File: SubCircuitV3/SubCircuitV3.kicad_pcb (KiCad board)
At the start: 2 copper layers, 120 x 120.1 mm, 26 parts, among them J1 JTAG, J10 ESC_POWER, J11 ESC_POWER, J12 ESC_POWER, J13 ESC_POWER, J14 FEMALE XT-60, J15 ESC PWM, J16 3S, J2 ESC PWM, J3 ESC PWM, J4 ESC PWM, J5 ESC PWM, J6 ESC PWM, J7 5S, J8 ESC_POWER, J9 ESC_POWER, K1 G5Q-1A

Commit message: Finalized V3 Board
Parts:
- added R3: 1000, Resistor_THT:R_Axial_DIN0207_L6.3mm_D2.5mm_P10.16mm_Horizontal, F.Cu at (107.3, 124.1)
- R1: value 2000 -> 1000
- moved R1 12.5 mm to (111.4, 124.1), turned to -90 degrees
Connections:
- J1 pad 14: Net-(CR1-INPUT) -> Net-(CR1-OUTPUT)
- R1 pad 1: +12V -> Net-(K1-Pad1)
- R1 pad 2: Net-(K1-Pad1) -> +12V
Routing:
- net +12V: track 424.2 -> 435.5 mm
- net Net-(K1-Pad1): track 17.1 -> 22.2 mm
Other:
- board size 120 x 120.1 mm -> 121.4 x 121.2 mm

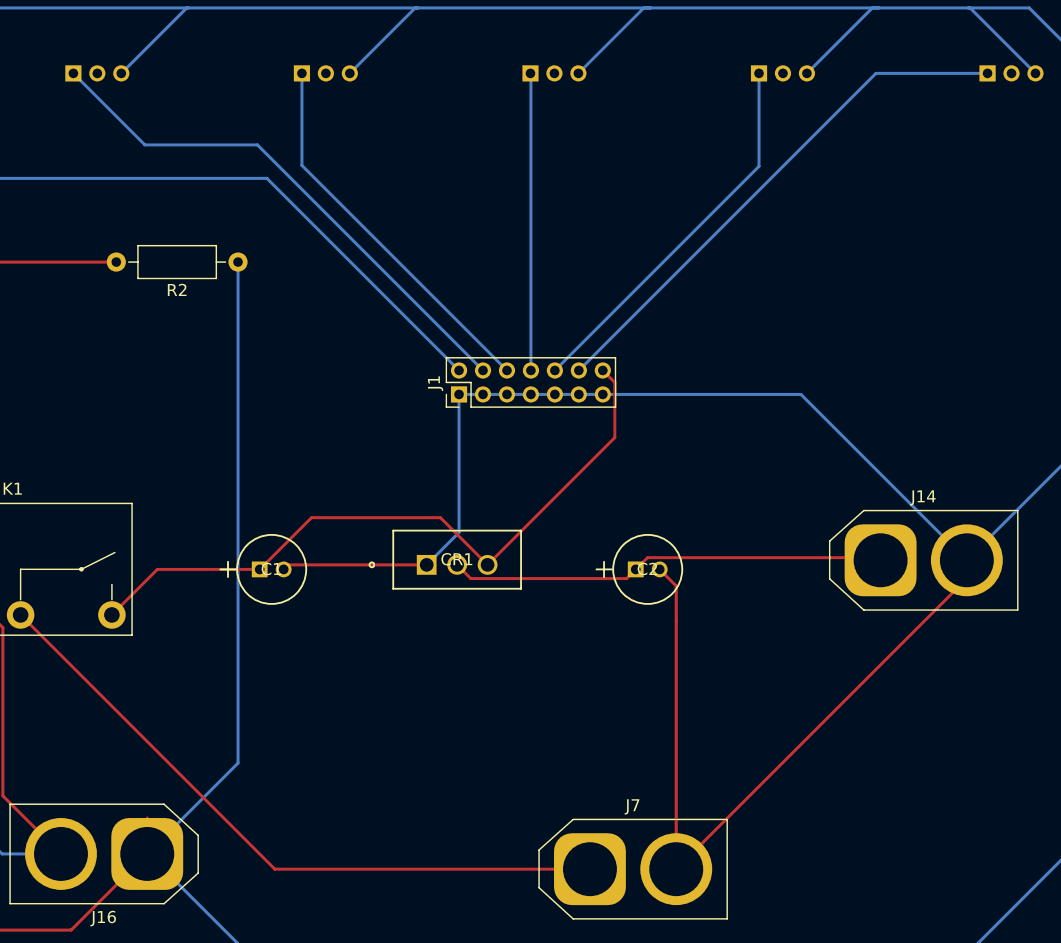
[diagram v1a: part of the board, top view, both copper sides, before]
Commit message: Added water sensors and fixed JTAG-Capacitor connection error
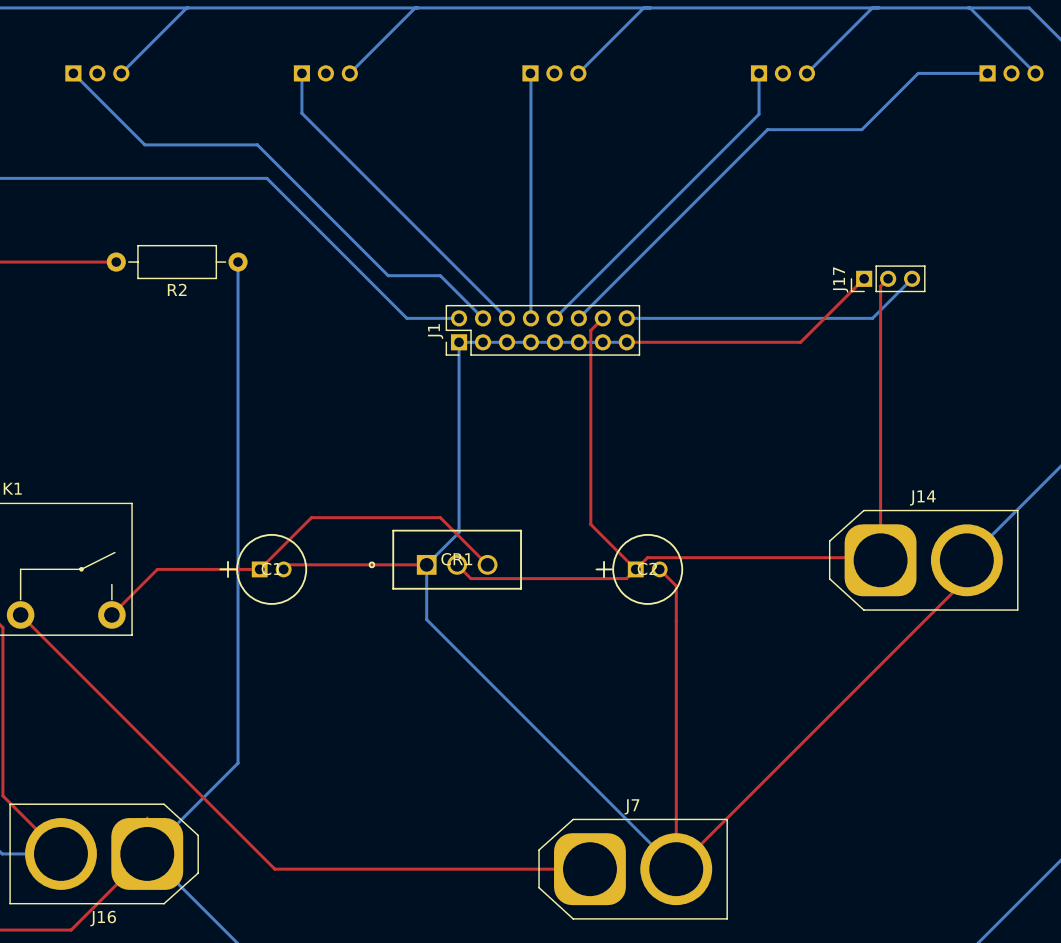
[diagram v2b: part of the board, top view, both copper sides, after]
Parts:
- added J17: Water Sensor Input, Connector_PinHeader_2.00mm:PinHeader_1x03_P2.00mm_Vertical, F.Cu at (196.8, 79.9)
- J1: footprint Connector_PinHeader_2.00mm:PinHeader_2x07_P2.00mm_Vertical -> Connector_PinHeader_2.00mm:PinHeader_2x08_P2.00mm_Vertical
- moved J1 4.35 mm to (163.0, 85.2)
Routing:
- net Net-(CR1-OUTPUT): track 36.6 -> 83.3 mm
- net GND2: track 326.2 -> 352.5 mm
- net Net-(J1-Pin_16): track 0.00 -> 25.2 mm
- net Net-(CR1-INPUT): track 57.4 -> 36.3 mm
- net Net-(J1-Pin_10): track 31.9 -> 27.5 mm
- net Net-(J1-Pin_6): track 31.9 -> 27.7 mm
- net Net-(J1-Pin_8): track 24.9 -> 20.7 mm
- net Net-(J1-Pin_4): track 44.5 -> 42.7 mm
- net Net-(J1-Pin_2): track 61.5 -> 59.7 mm
- net Net-(J1-Pin_12): track 44.4 -> 42.6 mm

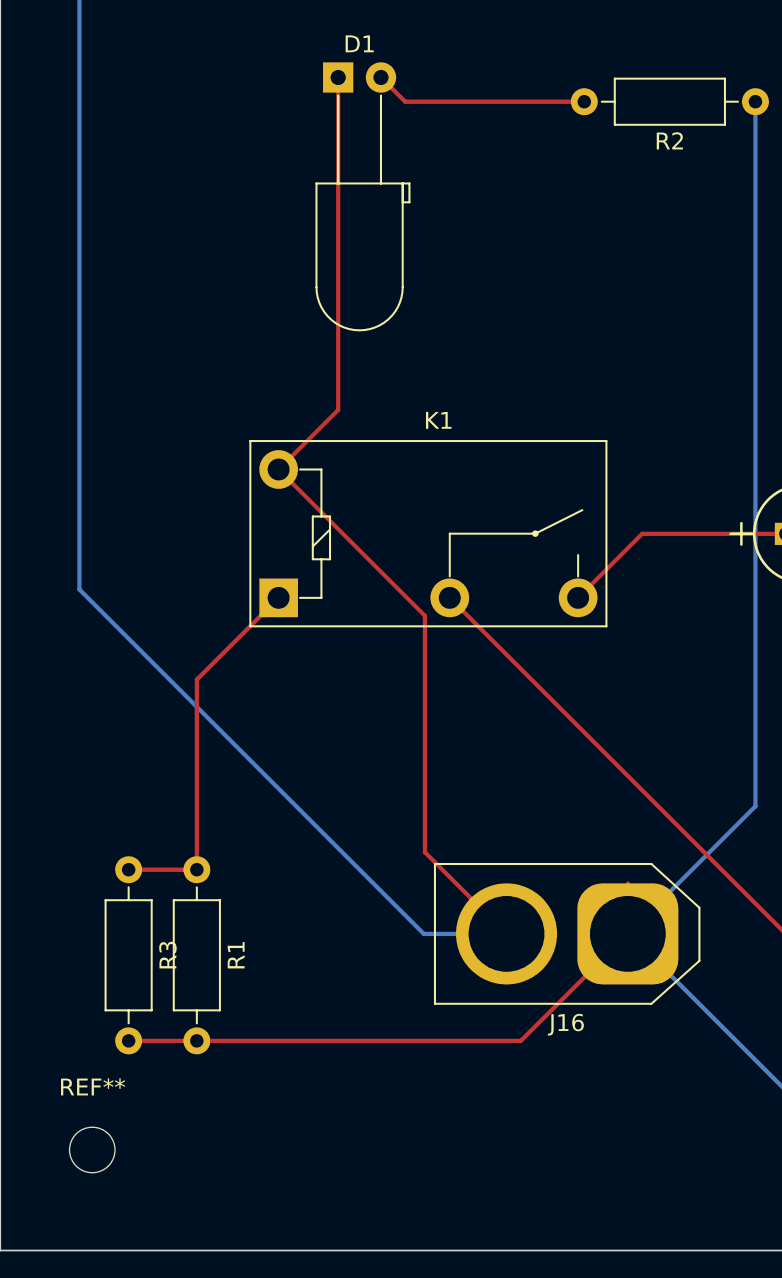
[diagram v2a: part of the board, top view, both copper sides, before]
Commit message: Added mosfet
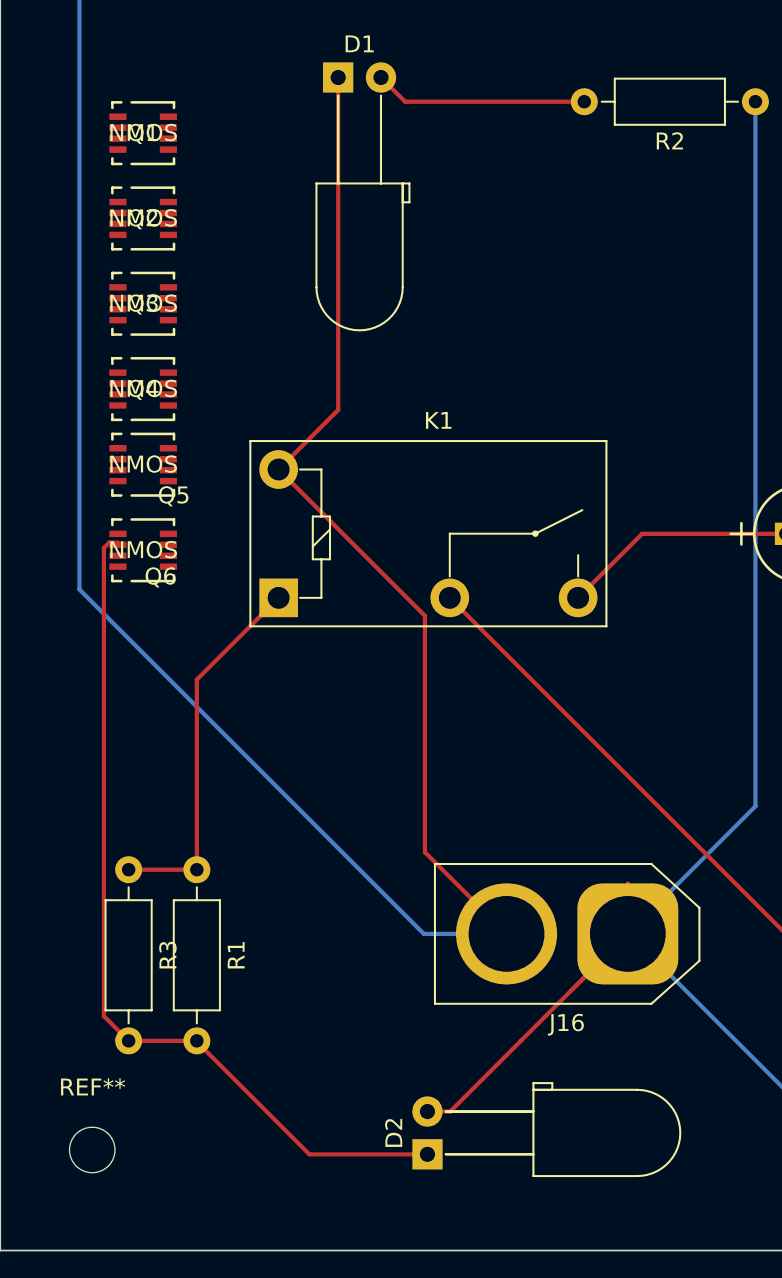
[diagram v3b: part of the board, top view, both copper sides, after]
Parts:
- added D2: switch, LED_THT:LED_D5.0mm_Horizontal_O6.35mm_Z9.0mm, F.Cu at (125.1, 141.0)
- added Q1: NMOS, BSZ065N03LSATMA1-MOSFET:BSZ065N03LSATMA1, F.Cu at (108.2, 80.4)
- added Q2: NMOS, BSZ065N03LSATMA1-MOSFET:BSZ065N03LSATMA1, F.Cu at (108.2, 85.4)
- added Q3: NMOS, BSZ065N03LSATMA1-MOSFET:BSZ065N03LSATMA1, F.Cu at (108.2, 90.5)
- added Q4: NMOS, BSZ065N03LSATMA1-MOSFET:BSZ065N03LSATMA1, F.Cu at (108.2, 95.5)
- added Q5: NMOS, BSZ065N03LSATMA1-MOSFET:BSZ065N03LSATMA1, F.Cu at (108.2, 100.0)
- added Q6: NMOS, BSZ065N03LSATMA1-MOSFET:BSZ065N03LSATMA1, F.Cu at (108.2, 105.1)
- C1, C2: footprint 860010372001:CAP_WCAP-ATG8_5x11_WRE -> Capacitor_WCAP-ATG8_5x11_WRE:CAP_WCAP-ATG8_5x11_WRE
- CR1: footprint LD1085V50_footprints:TO-220_STM -> LD1085V50:TO-220_STM
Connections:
- J10 pad 2: +12V -> Net-(J10-Pin_2)
- J11 pad 2: +12V -> Net-(J11-Pin_2)
- J12 pad 2: +12V -> Net-(J12-Pin_2)
- J13 pad 2: +12V -> Net-(J13-Pin_2)
- J8 pad 2: +12V -> Net-(J8-Pin_2)
- J9 pad 2: +12V -> Net-(J9-Pin_2)
- R1 pad 2: +12V -> /SG
- R3 pad 2: +12V -> /SG
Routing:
- net /SG: track 0.00 -> 50.8 mm
- net +12V: track 435.5 -> 424.2 mm

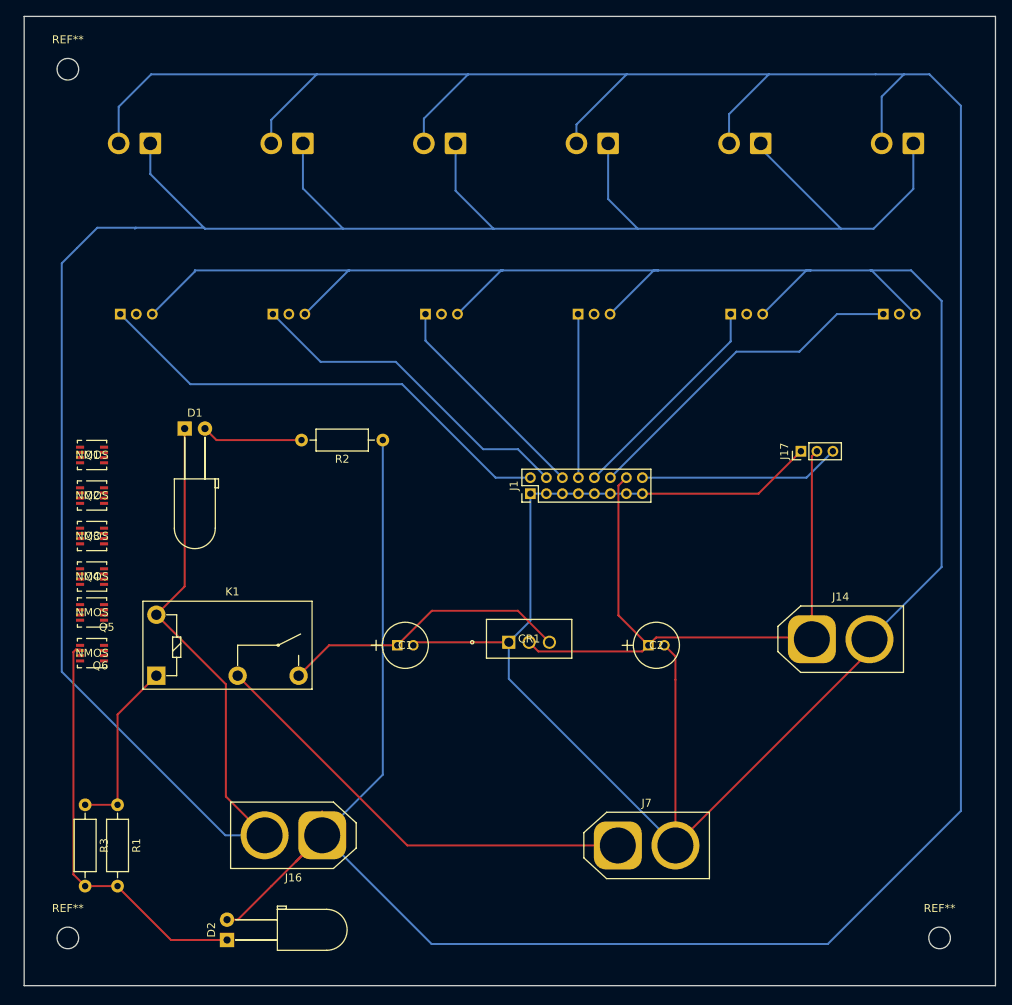
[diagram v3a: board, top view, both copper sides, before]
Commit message: Added fuses, mosfets, and updated power ports
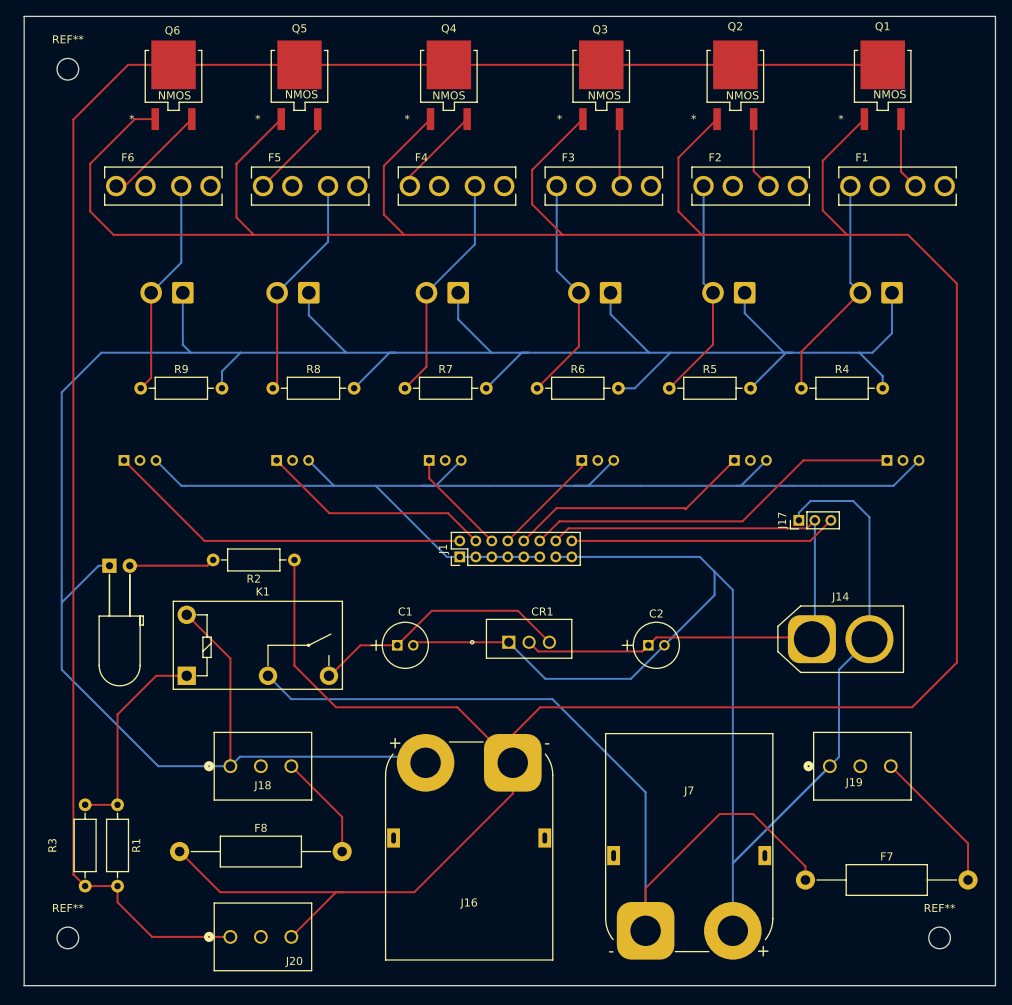
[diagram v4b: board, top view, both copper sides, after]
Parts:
- removed D2: switch, LED_THT:LED_D5.0mm_Horizontal_O6.35mm_Z9.0mm
- added F1: 3544-2, 3544-2:FUSE_3544-2, F.Cu at (208.9, 46.7)
- added F2: 3544-2, 3544-2:FUSE_3544-2, F.Cu at (190.5, 46.7)
- added F3: 3544-2, 3544-2:FUSE_3544-2, F.Cu at (172.2, 46.7)
- added F4: 3544-2, 3544-2:FUSE_3544-2, F.Cu at (153.8, 46.7)
- added F5: 3544-2, 3544-2:FUSE_3544-2, F.Cu at (135.4, 46.7)
- added F6: 3544-2, 3544-2:FUSE_3544-2, F.Cu at (117.1, 46.7)
- added F7: Fuse, Resistor_THT:R_Axial_DIN0411_L9.9mm_D3.6mm_P20.32mm_Horizontal, F.Cu at (197.4, 133.5)
- added F8: Fuse, Resistor_THT:R_Axial_DIN0411_L9.9mm_D3.6mm_P20.32mm_Horizontal, F.Cu at (119.1, 129.9)
- added J18: 3S OUT, 284932-3:CONN3_284392-3_TEC, F.Cu at (125.5, 119.3)
- added J19: 2S OUT, 284932-3:CONN3_284392-3_TEC, F.Cu at (200.4, 119.3)
- added J20: SWITCH, 284932-3:CONN3_284392-3_TEC, F.Cu at (125.5, 140.6)
- added R4: R, Resistor_THT:R_Axial_DIN0207_L6.3mm_D2.5mm_P10.16mm_Horizontal, F.Cu at (196.8, 72.0)
- added R5: R, Resistor_THT:R_Axial_DIN0207_L6.3mm_D2.5mm_P10.16mm_Horizontal, F.Cu at (180.3, 72.0)
- added R6: R, Resistor_THT:R_Axial_DIN0207_L6.3mm_D2.5mm_P10.16mm_Horizontal, F.Cu at (163.8, 72.0)
- added R7: R, Resistor_THT:R_Axial_DIN0207_L6.3mm_D2.5mm_P10.16mm_Horizontal, F.Cu at (147.3, 72.0)
- added R8: R, Resistor_THT:R_Axial_DIN0207_L6.3mm_D2.5mm_P10.16mm_Horizontal, F.Cu at (130.8, 72.0)
- added R9: R, Resistor_THT:R_Axial_DIN0207_L6.3mm_D2.5mm_P10.16mm_Horizontal, F.Cu at (114.3, 72.0)
- J16: value 3S -> 5S; footprint AMASS_XT60-M:AMASS_XT60-M_1x02_P7.20mm_Vertical -> Connector_AMASS:AMASS_XT90PW-M_1x02_P10.90mm_Horizontal
- J7: value 5S -> 3S; footprint AMASS_XT60-M:AMASS_XT60-M_1x02_P7.20mm_Vertical -> Connector_AMASS:AMASS_XT90PW-M_1x02_P10.90mm_Horizontal
- Q1, Q2, Q3, Q4, Q5, Q6: footprint BSZ065N03LSATMA1-MOSFET:BSZ065N03LSATMA1 -> AOD454:AOD454A
- moved Q1 109.6 mm to (207.0, 33.0)
- moved Q2 96.0 mm to (188.6, 33.0)
- moved Q3 85.8 mm to (171.8, 33.0)
- moved Q4 76.8 mm to (152.8, 33.0)
- moved Q6 72.8 mm to (118.4, 33.0)
- moved Q5 71.9 mm to (134.1, 33.0)
- moved J16 25.5 mm to (160.8, 118.8)
- moved D1 19.6 mm to (110.4, 94.2)
- moved J13 19.1 mm to (119.5, 60.1)
- moved J8 18.9 mm to (208.2, 60.1)
- moved J9 18.8 mm to (189.8, 60.1)
- moved J12 18.7 mm to (135.3, 60.1)
- moved J11 18.7 mm to (153.9, 60.1)
- moved J10 18.7 mm to (173.0, 60.1)
- moved R2 18.6 mm to (133.5, 93.5)
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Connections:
- J1 pad 1: GND2 -> GNDS
- J1 pad 11: GND2 -> GNDS
- J1 pad 3: GND2 -> GNDS
- J1 pad 5: GND2 -> GNDS
- J1 pad 7: GND2 -> GNDS
- J1 pad 9: GND2 -> GNDS
- J15 pad 3: GND2 -> GNDS
- J2 pad 3: GND2 -> GNDS
- J3 pad 3: GND2 -> GNDS
- J4 pad 3: GND2 -> GNDS
- J5 pad 3: GND2 -> GNDS
- J6 pad 3: GND2 -> GNDS
- Q1 pad 3: Net-(J8-Pin_2) -> Net-(Q1-S)
- Q2 pad 3: Net-(J9-Pin_2) -> Net-(Q2-S)
- Q3 pad 3: Net-(J10-Pin_2) -> Net-(Q3-S)
- Q4 pad 3: Net-(J11-Pin_2) -> Net-(Q4-S)
- Q5 pad 3: Net-(J12-Pin_2) -> Net-(Q5-S)
- Q6 pad 3: Net-(J13-Pin_2) -> Net-(Q6-S)
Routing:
- net /SG: track 50.8 -> 223.1 mm
- net GND2: track 352.5 -> 194.2 mm
- net GNDS: track 0.00 -> 144.2 mm
- net +7.5V: track 56.3 -> 104.1 mm
- net Net-(J11-Pin_2): track 0.00 -> 28.9 mm
- net Net-(J8-Pin_2): track 0.00 -> 28.8 mm
- net Net-(J10-Pin_2): track 0.00 -> 28.6 mm
- net Net-(J12-Pin_2): track 0.00 -> 28.1 mm
- net Net-(J9-Pin_2): track 0.00 -> 28.0 mm
- net Net-(J13-Pin_2): track 0.00 -> 27.4 mm
- net Net-(J19-Pin_3): track 0.00 -> 18.2 mm
- net Net-(J1-Pin_6): track 27.7 -> 13.3 mm
- net Net-(J1-Pin_2): track 59.7 -> 46.1 mm
- net Net-(J18-Pin_3): track 0.00 -> 13.3 mm
- net Net-(Q6-S): track 0.00 -> 12.9 mm
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
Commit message: Larger routing wires
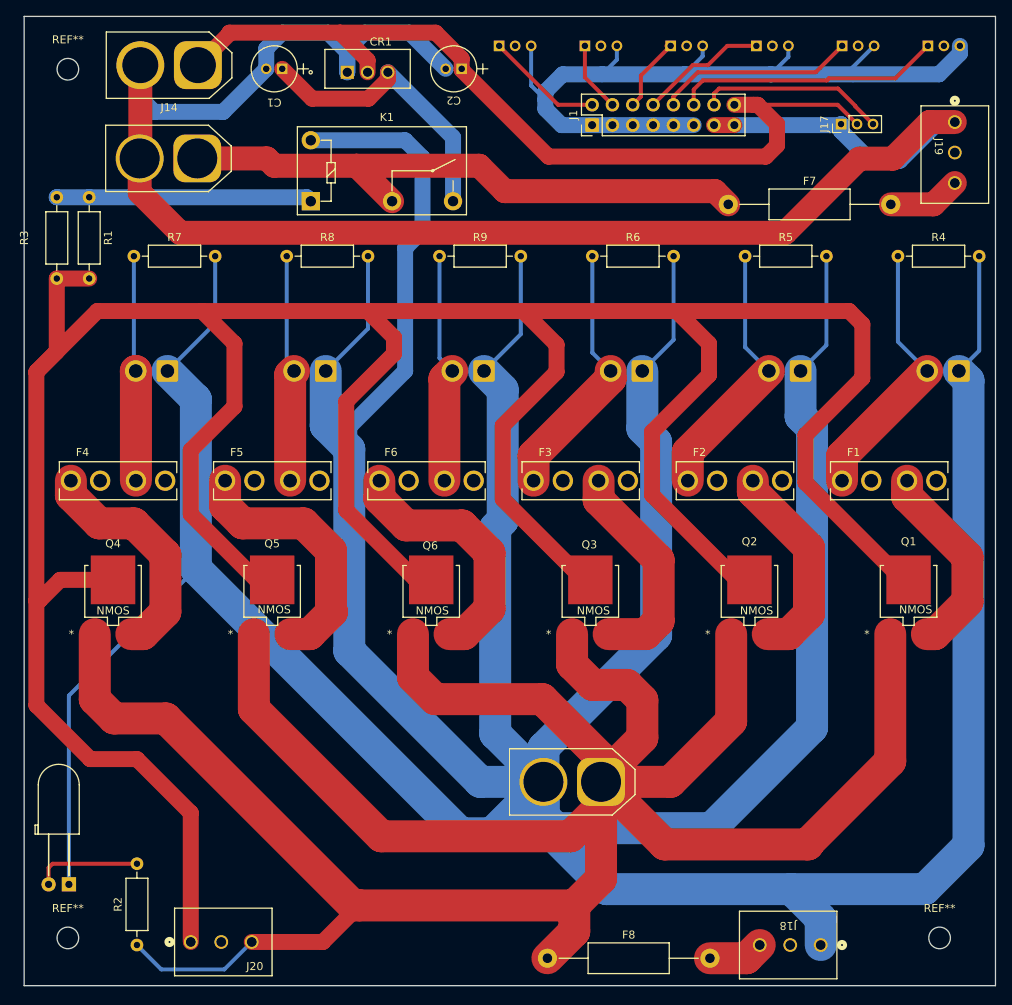
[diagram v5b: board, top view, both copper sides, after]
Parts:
- J1: footprint Connector_PinHeader_2.00mm:PinHeader_2x08_P2.00mm_Vertical -> Connector_PinHeader_2.54mm:PinHeader_2x08_P2.54mm_Vertical
- J16, J7: footprint Connector_AMASS:AMASS_XT90PW-M_1x02_P10.90mm_Horizontal -> Footprints:XT90
- moved J7 113.4 mm to (118.0, 43.2), turned to 180 degrees
- moved J14 105.1 mm to (121.4, 31.6), turned to 180 degrees
- moved F7 85.0 mm to (187.7, 49.0)
- moved J19 82.0 mm to (216.0, 38.7), turned to -90 degrees
- moved J18 77.1 mm to (199.3, 141.6), turned to 180 degrees
- moved Q4 76.9 mm to (110.8, 97.4)
- moved R1 76.0 mm to (107.8, 48.1)
- moved R3 76.0 mm to (103.8, 48.1)
- moved C2 75.7 mm to (154.4, 32.1), turned to 180 degrees
- moved CR1 74.1 mm to (140.1, 32.5)
- moved C1 73.5 mm to (132.0, 32.1), turned to 180 degrees
- moved Q6 72.0 mm to (150.6, 97.4)
- moved J6 69.9 mm to (159.1, 29.2)
- moved J5 64.6 mm to (169.8, 29.2)
- moved Q5 64.5 mm to (130.7, 97.4)
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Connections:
- J1 pad 14: Net-(CR1-OUTPUT) -> Net-(J1-Pin_14)
- J1 pad 16: Net-(J1-Pin_16) -> Net-(CR1-OUTPUT)
- J17 pad 3: Net-(J1-Pin_16) -> Net-(J1-Pin_14)
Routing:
- net GND1: track 313.0 -> 685.5 mm
- net /SG: track 223.1 -> 431.1 mm
- net +12V: track 435.5 -> 352.7 mm
- net GNDS: track 144.2 -> 101.7 mm
- net Net-(J1-Pin_16): track 33.5 -> 0.00 mm
- net Net-(J1-Pin_2): track 46.1 -> 14.7 mm
- net +7.5V: track 104.1 -> 75.0 mm
- net Net-(CR1-OUTPUT): track 85.1 -> 111.3 mm
- net GND2: track 194.2 -> 220.3 mm
- net Net-(J1-Pin_14): track 0.00 -> 23.4 mm
- net Net-(Q5-S): track 11.2 -> 32.7 mm
- net Net-(J1-Pin_4): track 29.7 -> 8.79 mm
- net Net-(Q6-S): track 12.9 -> 32.1 mm
- net Net-(Q3-S): track 8.48 -> 27.6 mm
- net Net-(Q4-S): track 11.3 -> 29.2 mm
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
